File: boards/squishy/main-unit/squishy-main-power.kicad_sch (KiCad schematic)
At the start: 165 parts, among them J5 Jack-DC, Q1 NTMFS5C442NT1G, Q10 PFET, Q2 NX6008NBKR, Q3 NX6008NBKR, Q4 NX6008NBKR, Q5 NX6008NBKR, Q6 PMPB20EN, Q8 DMN65D8L-7, SW1 RST, U1 LFE5UM5G-45F-8BG381C, U13 LM51551DSSR, U18 HyperRAM, U19 HyperRAM, U2 GD25Q64EWIGR, U21 AP3428/A, U23 TLV62084ADSGR, U5 APX811-40UG-7, U8 TPS7A1125PDRVT, U9 TPS7A1112PDRVT

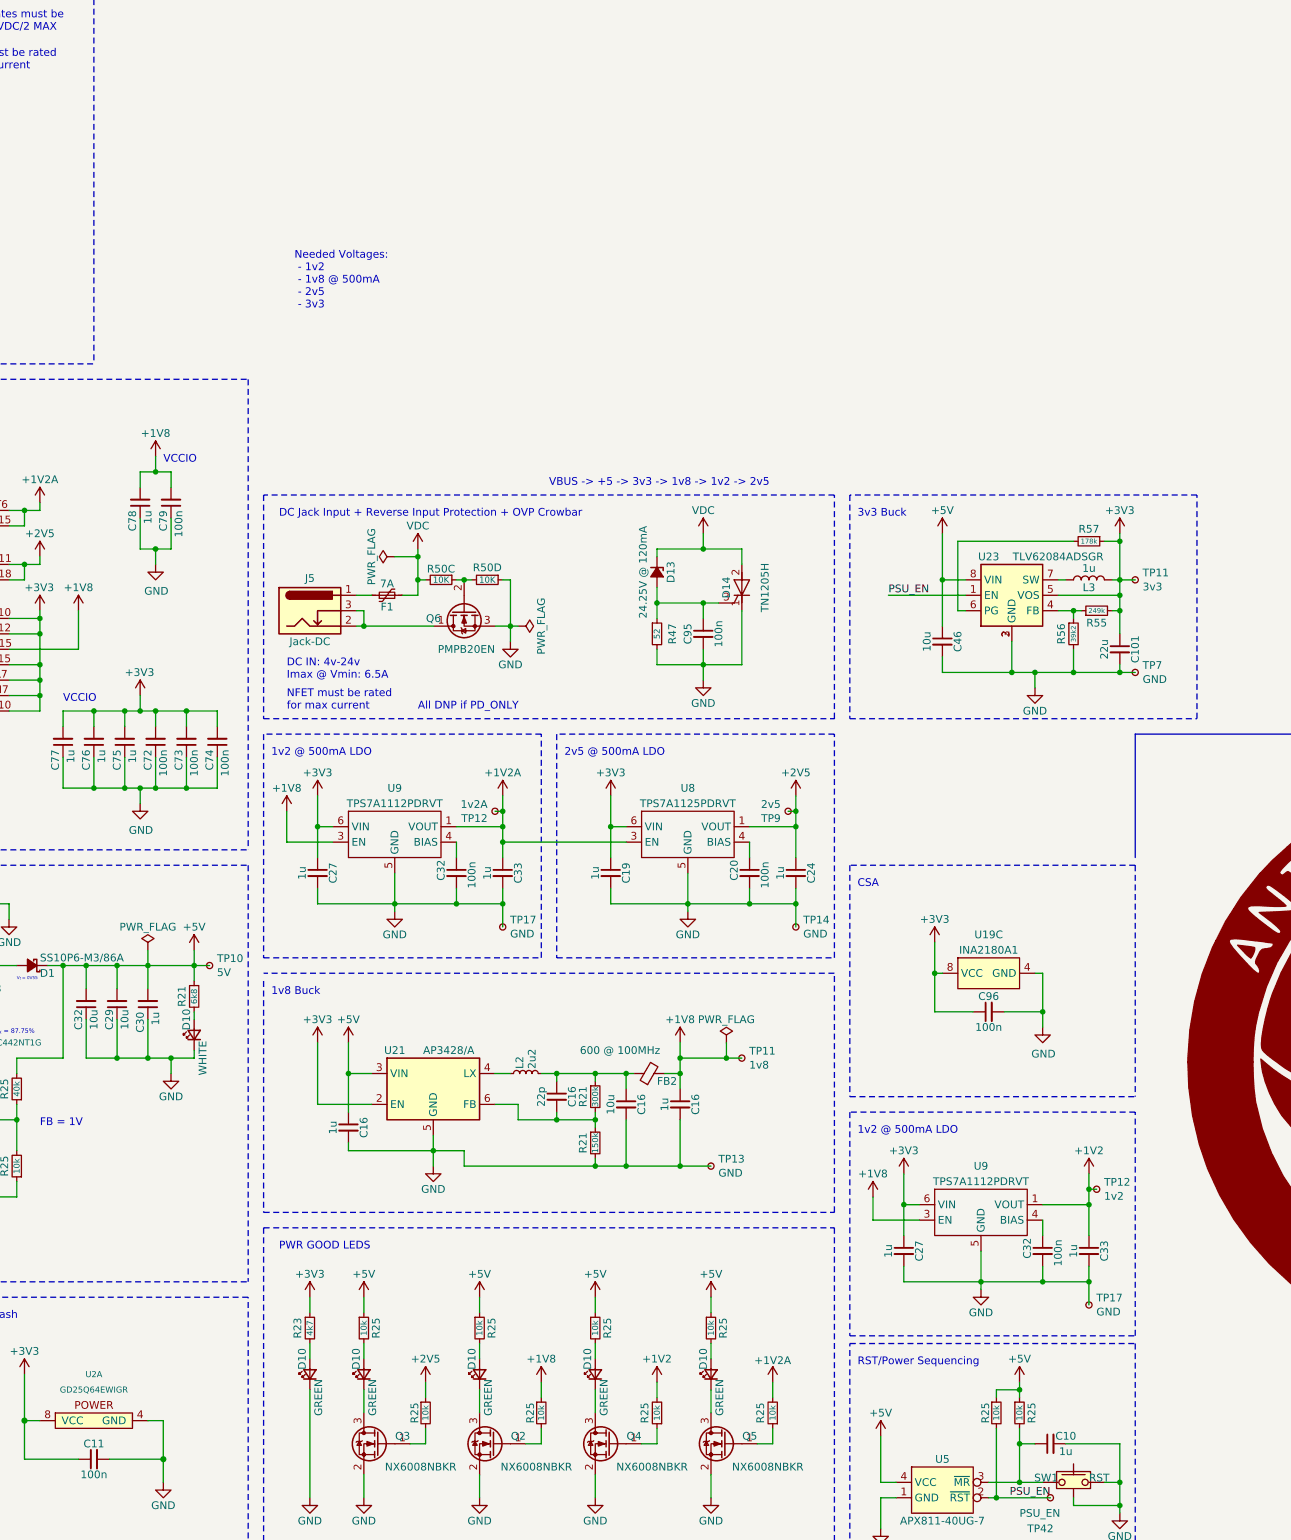
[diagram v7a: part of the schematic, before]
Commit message: squishy: main: some misc cleanup and tidying
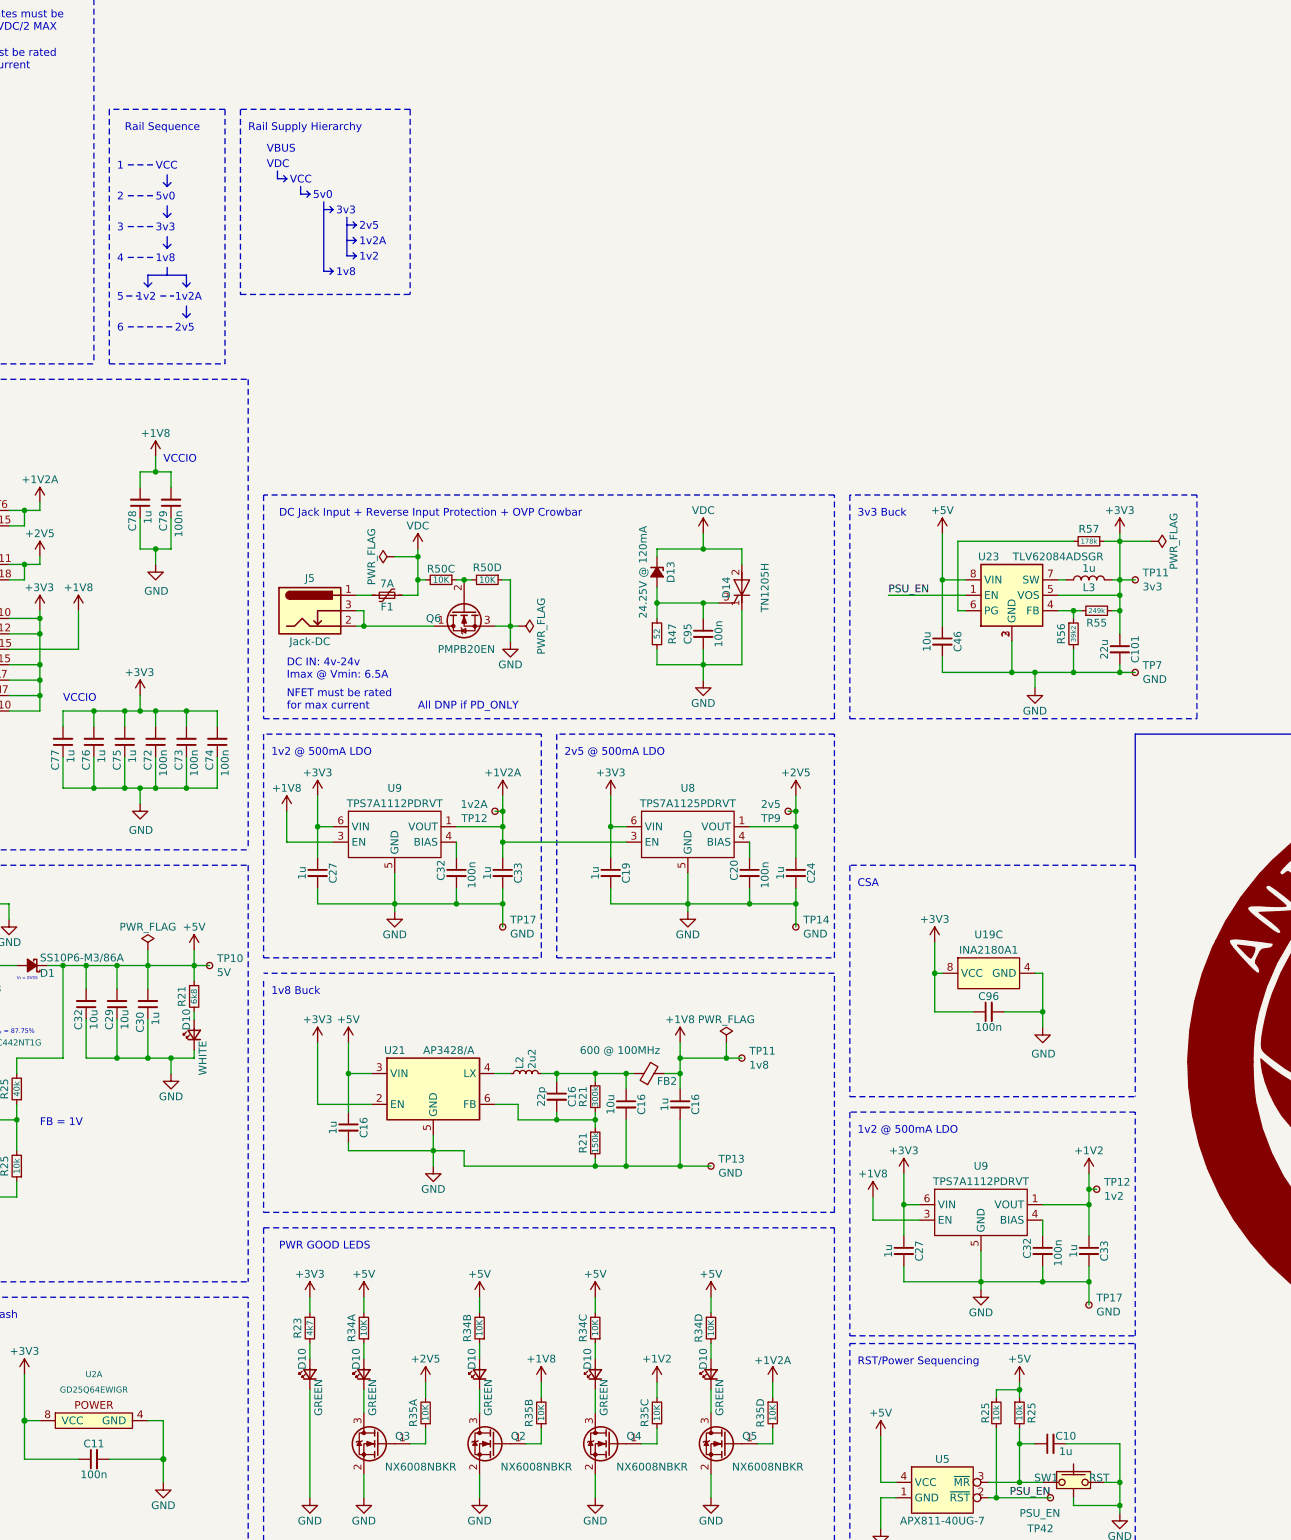
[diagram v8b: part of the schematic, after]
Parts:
- removed R25 (x8): 10k, Resistor_SMD:R_0603_1608Metric, symbol Device:R_Small
- added R34, R35: 10K, rhais_rcl:R0603_Array_Concave_4, symbol DX-MON:pkl_R4_Small
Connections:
- net +1V2: now also R35.6
- net +1V2A: now also R35.7
- net +1V8: now also R35.4
- net +2V5: now also R35.2
- net +5V: now also R34.2, R34.4, R34.6, R34.7
- net at Q5.1 (G): now also R35.8
- net at D10.2 (A): now also R34.1
- net at D10.2 (A): now also R34.3
- net at Q4.1 (G): now also R35.5
- net at D10.2 (A): now also R34.8
- net at Q2.1 (G): now also R35.3
- net at D10.2 (A): now also R34.5
- net at Q3.1 (G): now also R35.1
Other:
- note added: "1"
- note added: "1v2A"
- note added: "1v8"
- note added: "2"
- note added: "3"
- note added: "4"
- note added: "5"
- note added: "5v0"
- note added: "6"
- note added: "Rail Sequence"
- note added: "Rail Supply Hierarchy"
- note added: "VBUS"
- note added: "VDC"
- note removed: "Needed Voltages: - 1v2 - 1v8 @ 500mA - 2v5 - 3v3"
- note removed: "VBUS -> +5 -> 3v3 -> 1v8 -> 1v2 -> 2v5"
